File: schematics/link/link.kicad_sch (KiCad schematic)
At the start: 25 parts, among them J1 ARJM11C7-114-BA-EW2, J2 S1, J3 S2, J4 SDI

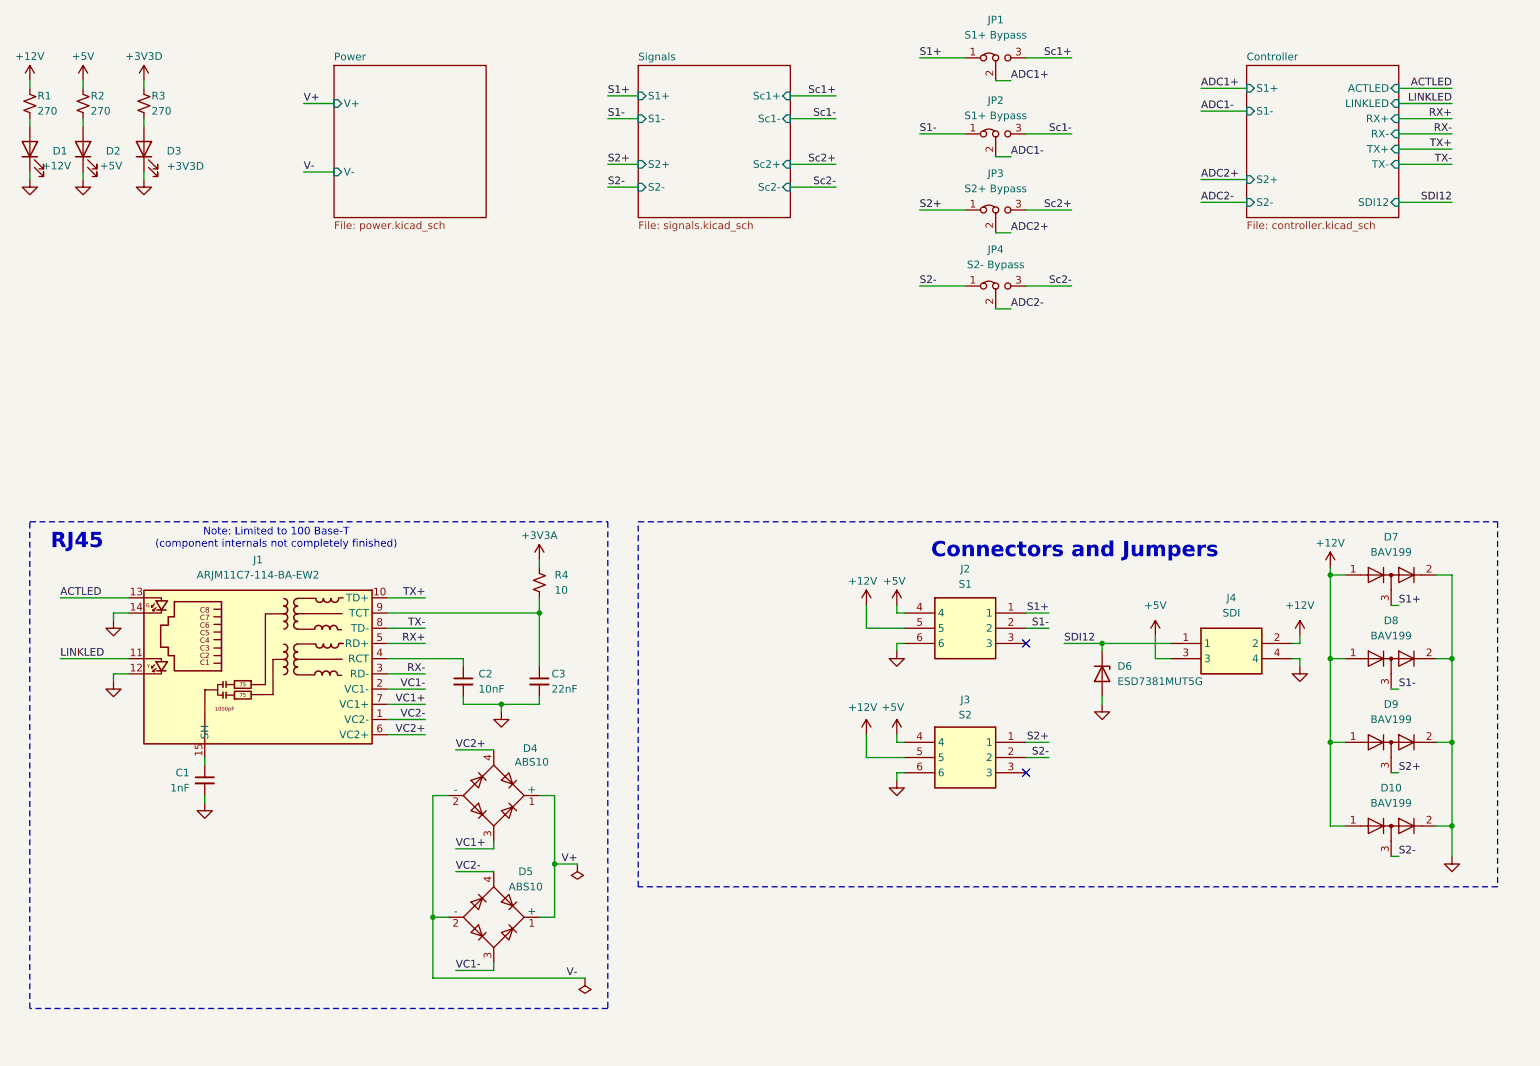
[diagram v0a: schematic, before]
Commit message: update(pcb): combining modules
Want to try a different layout, but like where I am at right now
Planning to branch off of this one and see where it goes
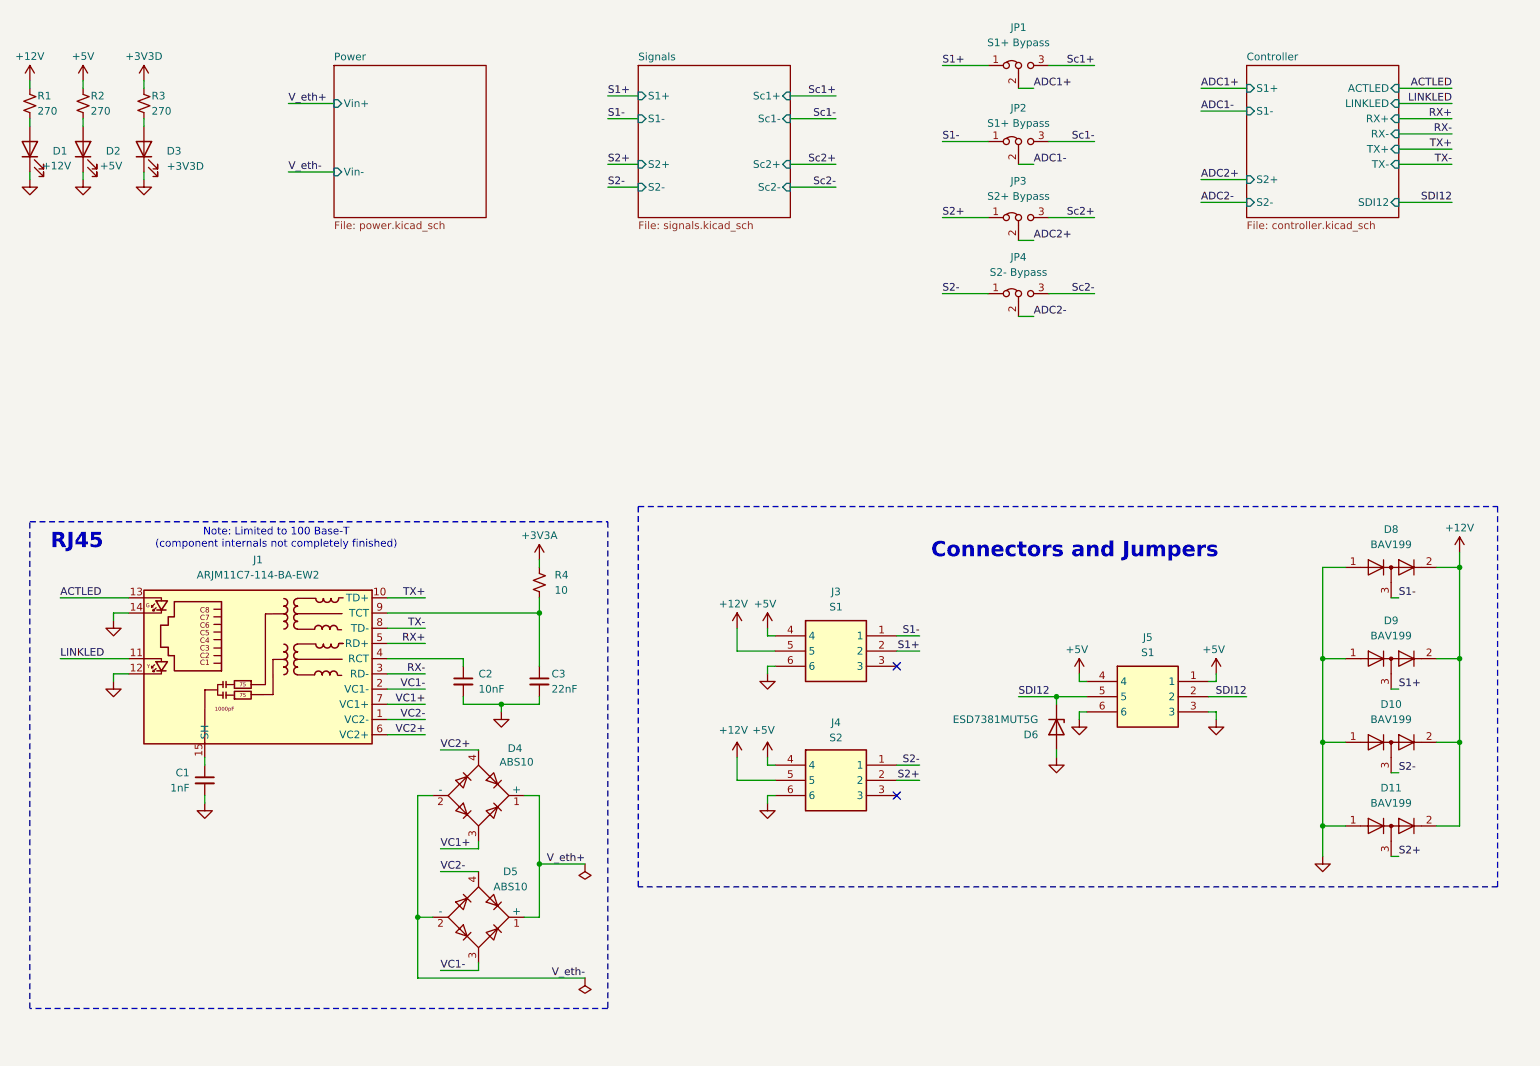
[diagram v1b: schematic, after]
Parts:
- removed J4: SDI, Link_Footprints:PC-1053864, symbol Link_Components:PC-1053864
- added J5: S1, Link_Footprints:PC-1053866, symbol Link_Components:PC-1818517
- C1, C2, C3: footprint Capacitor_SMD:C_0603_1608Metric -> Capacitor_SMD:C_0402_1005Metric
- J1: footprint Connector_RJ:RJ45_Abracon_ARJP11A-MA_Horizontal -> Link_Footprints:ARJM11C7-114-BA-EW2_ABR
- R1, R2, R3: footprint Resistor_SMD:R_0402_1005Metric -> Resistor_SMD:R_0603_1608Metric
- R4: footprint Resistor_SMD:R_0603_1608Metric -> Resistor_SMD:R_0402_1005Metric
- renumbered D9 to D10, D10 to D11, D7 to D8, D8 to D9, J2 to J3, J3 to J4
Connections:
- net +12V: now also D10.2 (A), D11.2 (A), D8.2 (A), D9.2 (A); no longer D10.1 (K), D11.1 (K), D8.1 (K), D9.1 (K)
- net +5V: now also J5.1, J5.4
- net GND: now also D10.1 (K), D11.1 (K), D8.1 (K), D9.1 (K), J5.3, J5.6; no longer D10.2 (A), D11.2 (A), D8.2 (A), D9.2 (A)
- net S1+: now also D9.3 (K), J3.2; no longer D8.3 (K), J3.1
- net S1-: now also D8.3 (K), J3.1; no longer D9.3 (K), J3.2
- net S2+: now also D11.3 (K), J4.2; no longer D10.3 (K), J4.1
- net S2-: now also D10.3 (K), J4.1; no longer D11.3 (K), J4.2
- net SDI12: now also J5.2, J5.5
- net V+ renamed V_eth+
- net V- renamed V_eth-
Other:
- sheet Power ports: added Vin+, Vin-; removed V+, V-
- moved on the sheet: D4, D5, D8, J3, J4, JP1, JP2, JP3, JP4

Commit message: update(link): finalized placements
Still some work to be done:
1. Fix planes under RJ45 connector, probably should keep out if possible
2. Fix silkscreening
3. Fix isolated filled zones
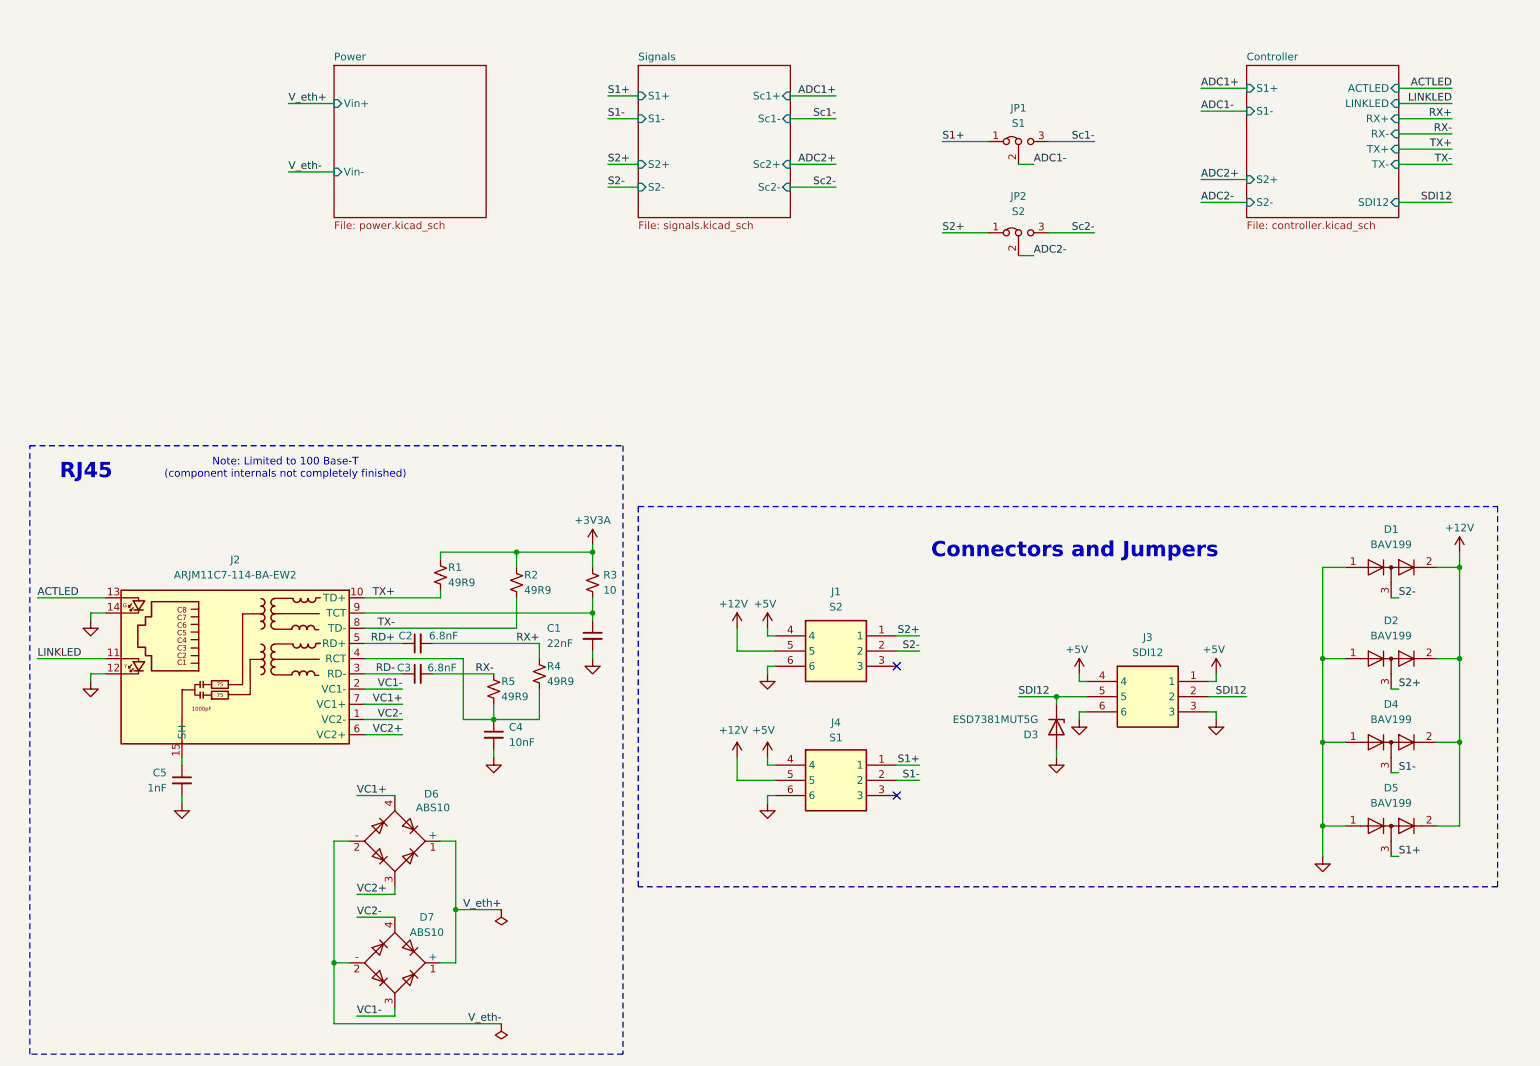
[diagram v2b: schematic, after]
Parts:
- removed D1: +12V, Diode_SMD:D_0603_1608Metric, symbol Device:LED
- removed D2: +5V, Diode_SMD:D_0603_1608Metric, symbol Device:LED
- removed D3: +3V3D, Diode_SMD:D_0603_1608Metric, symbol Device:LED
- removed JP1: S1+ Bypass, Connector_PinHeader_2.54mm:PinHeader_1x03_P2.54mm_Vertical, symbol Jumper:Jumper_3_Bridged12
- removed JP3: S2+ Bypass, Connector_PinHeader_2.54mm:PinHeader_1x03_P2.54mm_Vertical, symbol Jumper:Jumper_3_Bridged12
- removed R3: 270, Resistor_SMD:R_0603_1608Metric, symbol Device:R_Small_US
- added C3: 6.8nF, Capacitor_SMD:C_0402_1005Metric, symbol Device:C_Small
- added C4: 10nF, Capacitor_SMD:C_0402_1005Metric, symbol Device:C_Small
- added R4, R5: 49R9, Resistor_SMD:R_0402_1005Metric, symbol Device:R_Small_US
- C2: value 10nF -> 6.8nF
- J1: renamed from J3; value S1 -> S2
- J3: renamed from J5; value S1 -> SDI12
- J4: value S2 -> S1
- JP1: renamed from JP2; value S1+ Bypass -> S1
- JP2: renamed from JP4; value S2- Bypass -> S2
- R1, R2: value 270 -> 49R9; footprint Resistor_SMD:R_0603_1608Metric -> Resistor_SMD:R_0402_1005Metric; LCSC C11429 -> C22859
- renumbered C3 to C1, C1 to C5, D8 to D1, D9 to D2, D6 to D3, D10 to D4, D11 to D5, D4 to D6, D5 to D7, J1 to J2, R4 to R3
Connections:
- net +12V: no longer R1.1
- net +3V3A: now also R1.1, R2.1
- net +5V: no longer R2.1
- net GND: now also C4.2; no longer C2.2
- net RX+: now also C2.2, R4.1; no longer J2.5 (RD+)
- net RX-: now also C3.2, R5.1; no longer J2.3 (RD-)
- net S1+: now also D5.3 (K), J4.1, JP1.1 (A); no longer D2.3 (K), J1.2
- net S1-: now also D4.3 (K), J4.2; no longer D1.3 (K), J1.1, JP1.1 (A)
- net S2+: now also D2.3 (K), J1.1, JP2.1 (A); no longer D5.3 (K), J4.2
- net S2-: now also D1.3 (K), J1.2; no longer D4.3 (K), J4.1, JP2.1 (A)
- net TX+: now also R1.2
- net TX-: now also R2.2
- net VC1+: now also D6.4; no longer D6.3
- net VC2+: now also D6.3; no longer D6.4
- net at J2.4 (RCT): now also C4.1, R4.2, R5.2; no longer C2.1
- new net RD+: C2.1, J2.5 (RD+)
- new net RD-: C3.1, J2.3 (RD-)
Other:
- moved on the sheet: C1, C5, D6, D7, J2, JP2, R3

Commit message: update(link): GPT review
GPT suggested a few changes:
1. ADS131M02 RC input network (not added)
   this maybe should be added as DNP, but AFE already
   handles basic filtering

2. Reroute S2+ on top plane (added)
3. Ag9912 minumum load (added)
   The minimum load requirement is 100mA at 12V,
   I added an LED for a baseline minimum, but
   digital ICs should get to 100mA alone
4. Remove input select jumper for production (not added)
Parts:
- C5: value 1nF -> 1nF / 200V
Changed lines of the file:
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@@
 			)
 		)
-		(property "Value" "1nF"
+		(property "Value" "1nF / 200V"
 			(at 48.26 146.0562 0)
 			(show_name no)

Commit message: fix: git history
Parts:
- removed C5: 1nF / 200V, Capacitor_SMD:C_0402_1005Metric, symbol Device:C_Small
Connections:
- net GND: now also J2.15 (SH), J2.16 (SH)
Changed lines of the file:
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@@
 	(wire
 		(pts
-			(xy 50.8 140.97) (xy 50.8 142.24)
-		)
-		(stroke
-			(width 0)
-			(type default)
-		)
-	)
-	(wire
-		(pts
 			(xy 195.58 38.1) (xy 203.2 38.1)
 		)
@@
 	(wire
 		(pts
-			(xy 50.8 148.59) (xy 50.8 147.32)
+			(xy 50.8 140.97) (xy 50.8 143.51)
 		)
 		(stroke
@@
 	(symbol
 		(lib_id "power:GND")
-		(at 50.8 148.59 0)
+		(at 50.8 143.51 0)
 		(mirror y)
 		(unit 1)
@@
 		(dnp no)
 		(property "Reference" "#PWR017"
-			(at 50.8 154.94 0)
+			(at 50.8 149.86 0)
 			(hide yes)
 			(show_name no)
@@
 		)
 		(property "Value" "GND"
-			(at 50.8 152.4 0)
+			(at 50.8 147.32 0)
 			(hide yes)
 			(show_name no)
@@
 		)
 		(property "Footprint" ""
-			(at 50.8 148.59 0)
+			(at 50.8 143.51 0)
 			(hide yes)
 			(show_name no)
@@
 		)
 		(property "Datasheet" ""
-			(at 50.8 148.59 0)
+			(at 50.8 143.51 0)
 			(hide yes)
 			(show_name no)
@@
 		)
 		(property "Description" "Power symbol creates a global label with name \"GND\" , ground"
-			(at 50.8 148.59 0)
+			(at 50.8 143.51 0)
 			(hide yes)
 			(show_name no)
@@
 					(unit 1)
 				)
-			)
-		)
-	)
-	(symbol
-		(lib_id "Device:C_Small")
-		(at 50.8 144.78 0)
-		(mirror y)
-		(unit 1)
-		(body_style 1)
-		(exclude_from_sim no)
-		(in_bom yes)
-		(on_board yes)
-		(in_pos_files yes)
-		(dnp no)
-		(fields_autoplaced yes)
-		(property "Reference" "C5"
-			(at 48.26 143.5162 0)
-			(show_name no)
-			(do_not_autoplace no)
-			(effects
-				(font
-					(size 1.27 1.27)
-				)
-				(justify left)
-			)
-		)
-		(property "Value" "1nF / 200V"
-			(at 48.26 146.0562 0)
-			(show_name no)
-			(do_not_autoplace no)
-			(effects
-				(font
-					(size 1.27 1.27)
-				)
-				(justify left)
-			)
-		)
-		(property "Footprint" "Capacitor_SMD:C_0402_1005Metric"
-			(at 50.8 144.78 0)
-			(hide yes)
-			(show_name no)
-			(do_not_autoplace no)
-			(effects
-				(font
-					(size 1.27 1.27)
-				)
-			)
-		)
-		(property "Datasheet" ""
-			(at 50.8 144.78 0)
-			(hide yes)
-			(show_name no)
-			(do_not_autoplace no)
-			(effects
-				(font
-					(size 1.27 1.27)
-				)
-			)
-		)
-		(property "Description" "Unpolarized capacitor, small symbol"
-			(at 50.8 144.78 0)
-			(hide yes)
-			(show_name no)
-			(do_not_autoplace no)
-			(effects
-				(font
-					(size 1.27 1.27)
-				)
-			)
-		)
-		(property "FT Rotation Offset" ""
-			(at 50.8 144.78 0)
-			(hide yes)
-			(show_name no)
-			(do_not_autoplace no)
-			(effects
-				(font
-					(size 1.27 1.27)
-				)
-			)
-		)
-		(property "LCSC" "C1588 "
-			(at 50.8 144.78 0)
-			(hide yes)
-			(show_name no)
-			(do_not_autoplace no)
-			(effects
-				(font
-					(size 1.27 1.27)
-				)
-			)
-		)
-		(pin "1"
-		)
-		(pin "2"
-		)
-		(instances
-			(project "link"
-				(path "/e6a73b1b-9233-47b9-8d6b-253608bed688"
-					(reference "C5")
-					(unit 1)
-				)
